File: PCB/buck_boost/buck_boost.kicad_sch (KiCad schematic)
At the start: 56 parts, among them J1 VIN 10-24V, J2 VOUT, J3 VOUT, J4 VOUT, J5 VOUT, Q1 TK1R4S04PB, Q2 TK1R4S04PB, Q3 TK1R4S04PB, Q4 TK1R4S04PB, Q5 TK1R4S04PB, U1 LTC4359-MS8, U2 LT8392

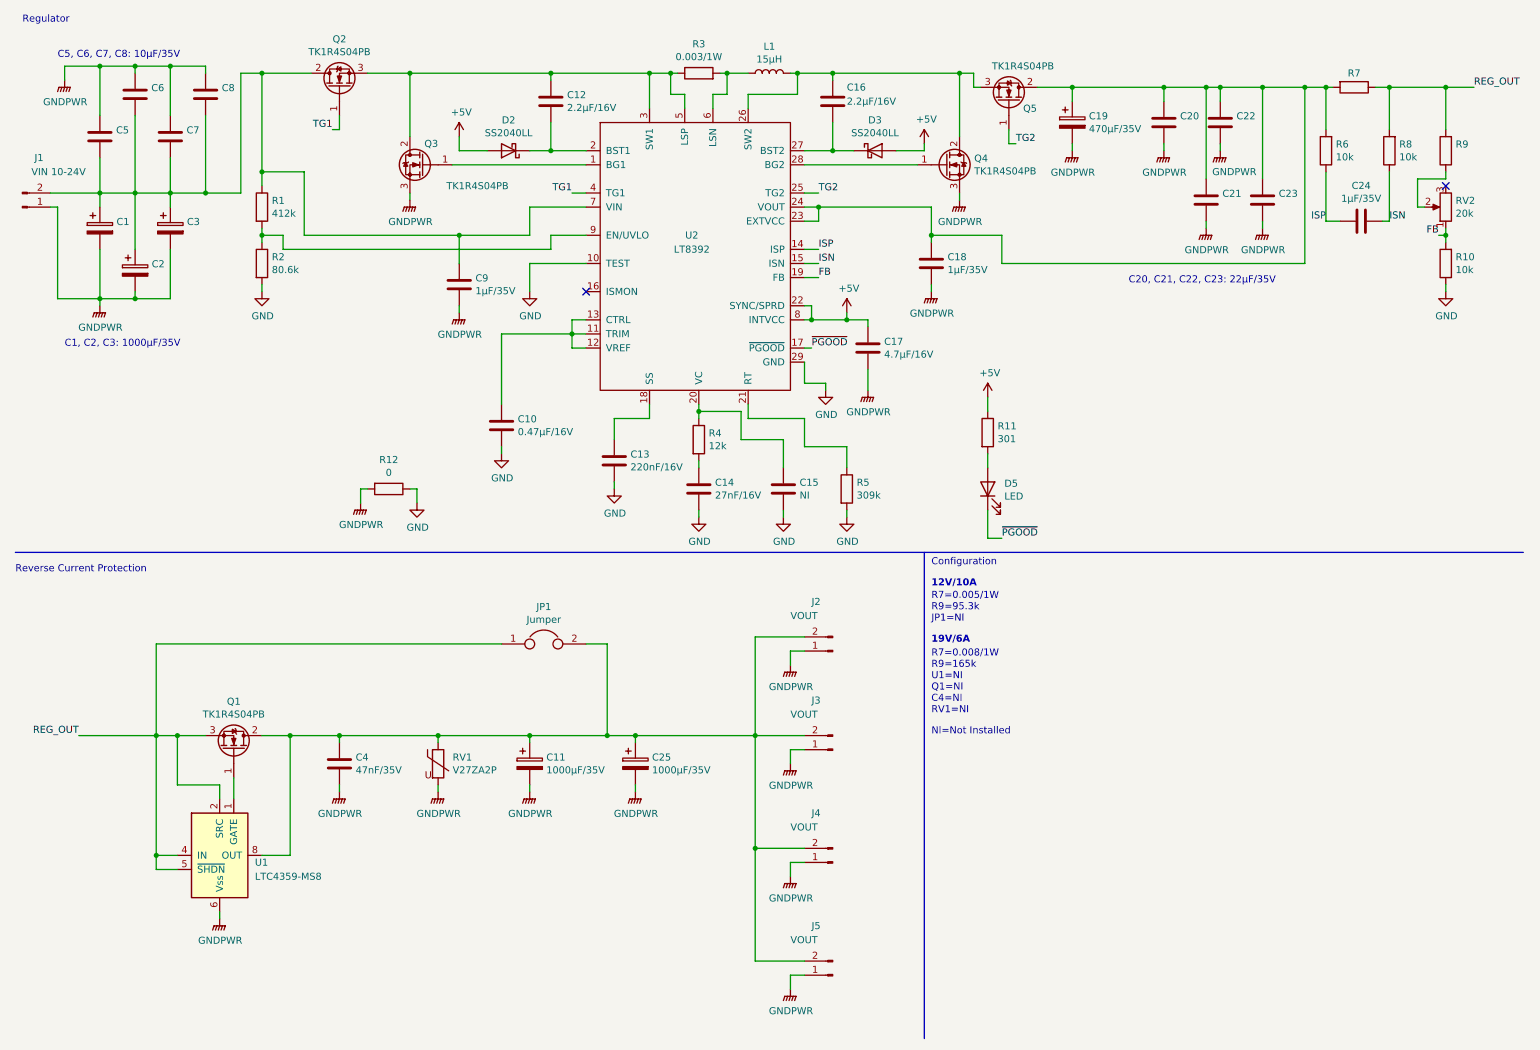
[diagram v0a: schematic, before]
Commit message: Add a PI filter to buck_boost. Fix ringing for other PI filters.
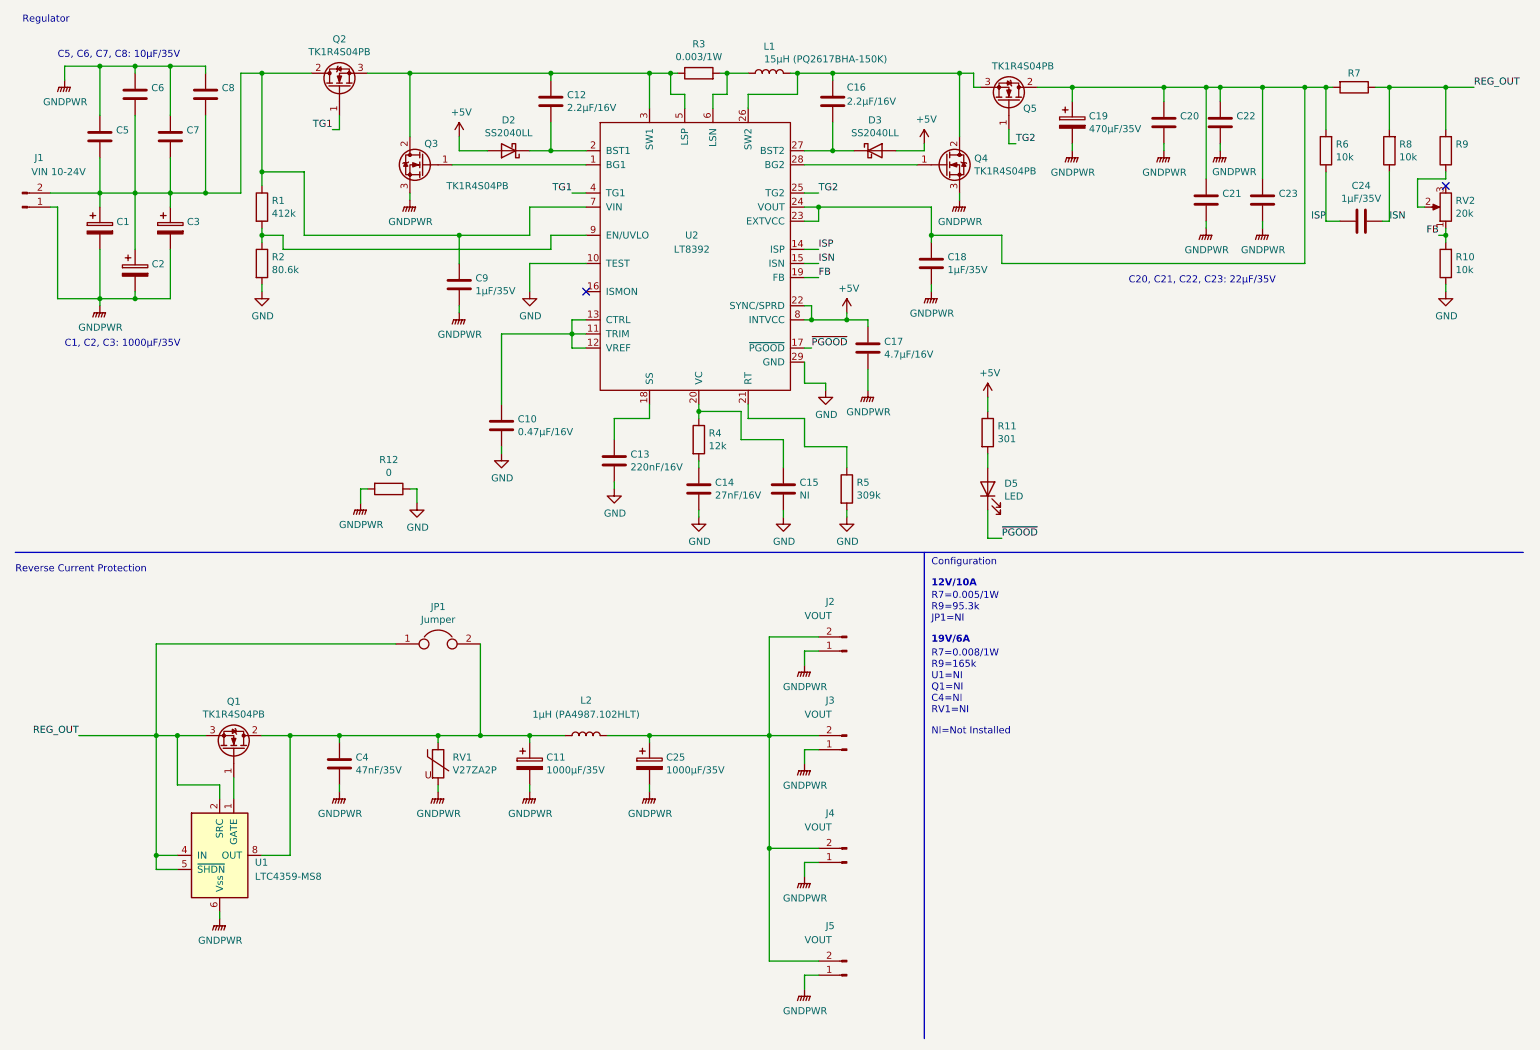
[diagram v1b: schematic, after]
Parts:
- added L2: 1µH (PA4987.102HLT), t-top:PA4987.XXXHL, symbol Device:L
- L1: value 15µH -> 15µH (PQ2617BHA-150K)
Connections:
- net at C11.1, C4.1, JP1.2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: now also L2.1; no longer C25.1, J2.2 (Pin_2), J3.2 (Pin_2), J4.2 (Pin_2), J5.2 (Pin_2)
- new net: C25.1, J2.2 (Pin_2), J3.2 (Pin_2), J4.2 (Pin_2), J5.2 (Pin_2), L2.2
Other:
- moved on the sheet: C25, J2, J3, J4, J5, JP1
